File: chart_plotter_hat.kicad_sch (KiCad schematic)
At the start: 70 parts, among them J1 JST PH, J10 JST PH, J11 Qwiic, J2 JST PH, J3 40HAT, J4 JST PH, J5 JST PH, J6 JST PH, J7 JST PH, J8 Conn_02x03_Odd_Even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

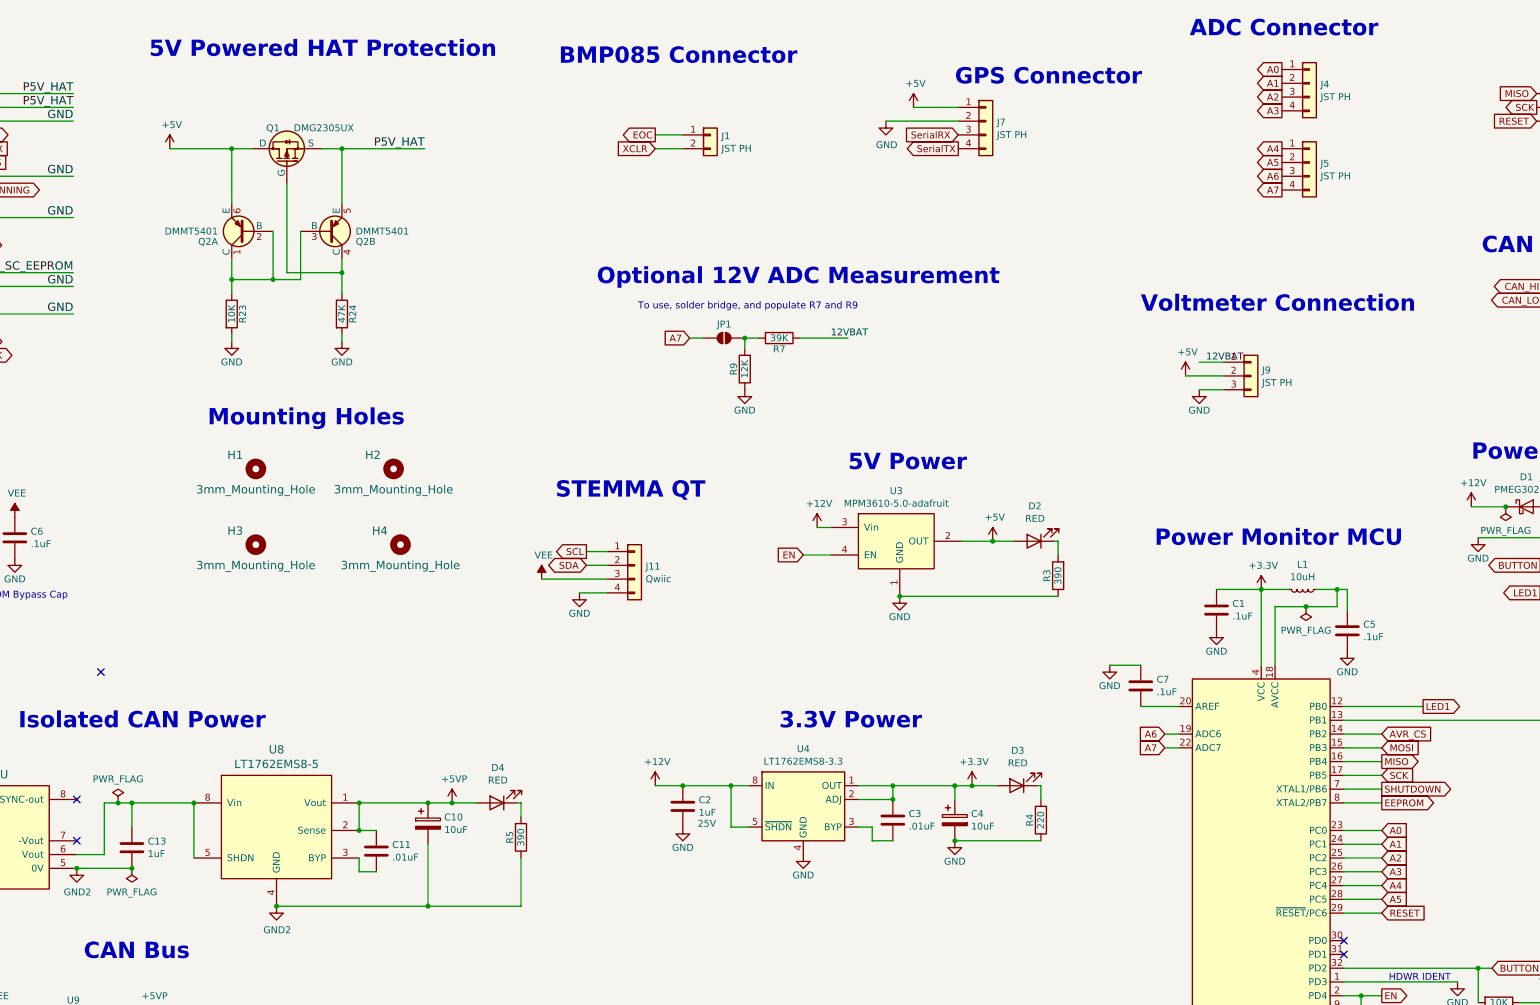
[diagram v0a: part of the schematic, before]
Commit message: Added solder jumpers for SCL/SDA
Removed BMP connector and associated routes
Can now connect QWIK connector to Pi or Atmega via jumpers
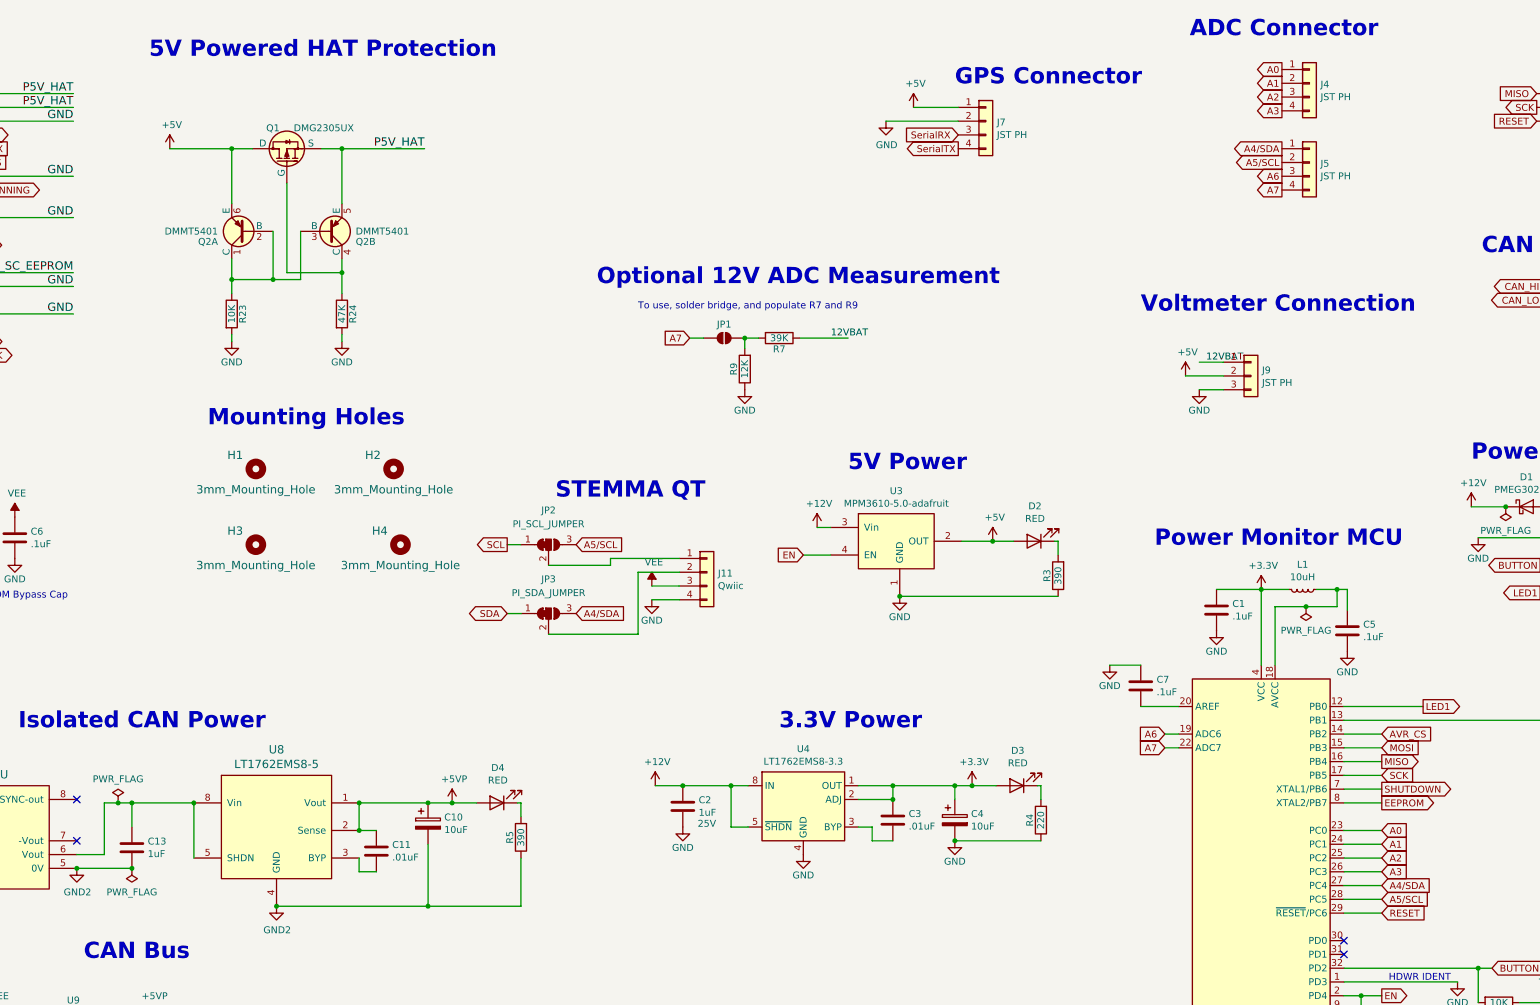
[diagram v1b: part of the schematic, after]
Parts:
- removed J1: JST PH, Connectors_JST:JST_PH_B2B-PH-K_02x2.00mm_Straight, symbol Connector_Generic:Conn_01x02
- added JP2: PI_SCL_JUMPER, Jumper:SolderJumper-3_P1.3mm_Bridged2Bar12_Pad1.0x1.5mm, symbol Jumper:SolderJumper_3_Bridged12
- added JP3: PI_SDA_JUMPER, Jumper:SolderJumper-3_P1.3mm_Bridged2Bar12_Pad1.0x1.5mm, symbol Jumper:SolderJumper_3_Bridged12
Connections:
- net SCL: now also JP2.1 (A); no longer J11.1 (Pin_1)
- net SDA: now also JP3.1 (A); no longer J11.2 (Pin_2)
- net A4 renamed A4/SDA
- net A4/SDA: now also JP3.3 (B)
- net A5 renamed A5/SCL
- net A5/SCL: now also JP2.3 (B)
- new net: J11.1 (Pin_1), JP2.2 (C)
- new net: J11.2 (Pin_2), JP3.2 (C)
- no-connect marks 28 -> 27
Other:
- note removed: "BMP085 Connector"
- moved on the sheet: J11

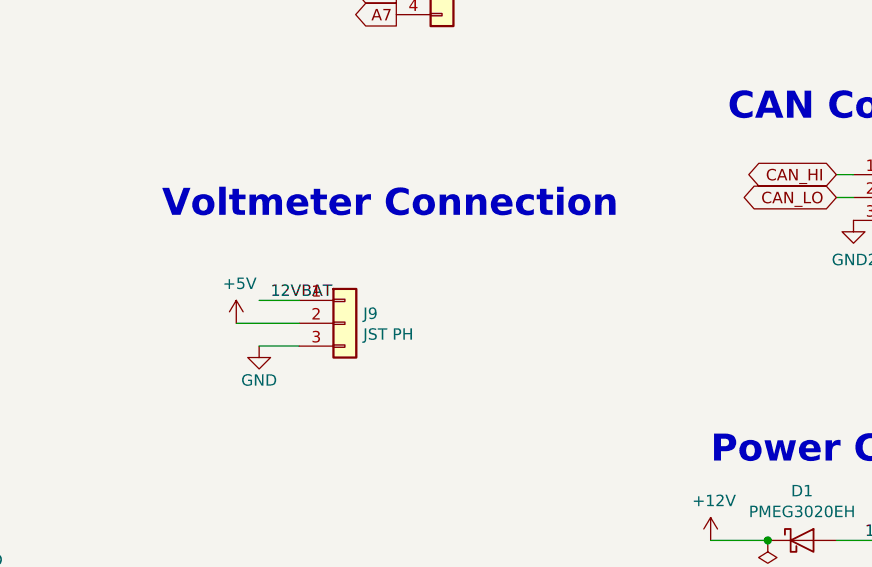
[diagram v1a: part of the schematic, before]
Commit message: Removed voltmeter connector and traces
Updated some trace routing
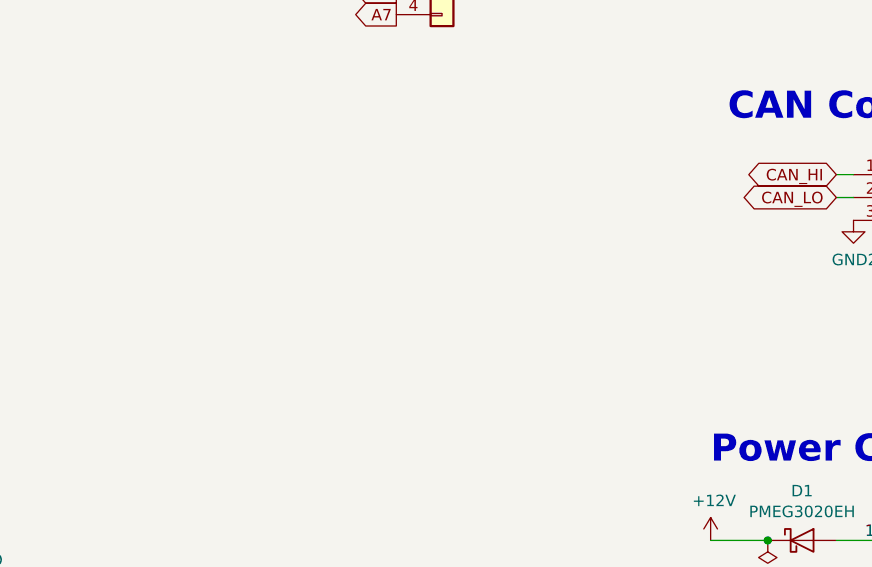
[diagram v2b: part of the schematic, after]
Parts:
- removed J9: JST PH, Connectors_JST:JST_PH_B3B-PH-K_03x2.00mm_Straight, symbol Connector_Generic:Conn_01x03
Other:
- note removed: "Voltmeter Connection"
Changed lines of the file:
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@@
 		)
 	)
-	(text "Voltmeter Connection"
-		(exclude_from_sim no)
-		(at 309.88 73.025 0)
-		(effects
-			(font
-				(size 2.9972 2.9972)
-				(thickness 0.5994)
-				(bold yes)
-			)
-			(justify left bottom)
-		)
-	)
 	(text "CAN Connector"
 		(exclude_from_sim no)
@@
 	(wire
 		(pts
-			(xy 325.12 86.995) (xy 320.675 86.995)
-		)
-		(stroke
-			(width 0)
-			(type default)
-		)
-	)
-	(wire
-		(pts
 			(xy 340.36 127) (xy 346.075 127)
 		)
@@
 	(wire
 		(pts
-			(xy 325.12 84.455) (xy 318.135 84.455)
-		)
-		(stroke
-			(width 0)
-			(type default)
-		)
-	)
-	(wire
-		(pts
 			(xy 82.55 40.005) (xy 91.44 40.005)
 		)
@@
 	(wire
 		(pts
-			(xy 325.12 81.915) (xy 320.675 81.915)
-		)
-		(stroke
-			(width 0)
-			(type default)
-		)
-	)
-	(wire
-		(pts
 			(xy 82.55 60.325) (xy 90.805 60.325)
 		)
@@
 		)
 	)
-	(label "12VBAT"
-		(at 321.945 81.915 0)
-		(effects
-			(font
-				(size 1.27 1.27)
-			)
-			(justify left bottom)
-		)
-	)
 	(label "GND"
 		(at 113.03 47.625 180)
@@
 	)
 	(symbol
-		(lib_id "Connector_Generic:Conn_01x03")
-		(at 330.2 84.455 0)
-		(unit 1)
-		(exclude_from_sim no)
-		(in_bom yes)
-		(on_board yes)
-		(dnp no)
-		(property "Reference" "J9"
-			(at 332.232 83.3882 0)
-			(effects
-				(font
-					(size 1.27 1.27)
-				)
-				(justify left)
-			)
-		)
-		(property "Value" "JST PH"
-			(at 332.232 85.6996 0)
-			(effects
-				(font
-					(size 1.27 1.27)
-				)
-				(justify left)
-			)
-		)
-		(property "Footprint" "Connectors_JST:JST_PH_B3B-PH-K_03x2.00mm_Straight"
-			(at 330.2 84.455 0)
-			(effects
-				(font
-					(size 1.27 1.27)
-				)
-				(hide yes)
-			)
-		)
-		(property "Datasheet" "~"
-			(at 330.2 84.455 0)
-			(effects
-				(font
-					(size 1.27 1.27)
-				)
-				(hide yes)
-			)
-		)
-		(property "Description" ""
-			(at 330.2 84.455 0)
-			(effects
-				(font
-					(size 1.27 1.27)
-				)
-			)
-		)
-		(pin "1"
-		)
-		(pin "2"
-		)
-		(pin "3"
-		)
-		(instances
-			(project ""
-				(path "/539f7589-5491-4018-9113-34d36da6b689"
-					(reference "J9")
-					(unit 1)
-				)
-			)
-		)
-	)
-	(symbol
 		(lib_id "Device:R")
 		(at 394.335 162.56 180)
@@
 	)
 	(symbol
-		(lib_id "power:GND")
-		(at 320.675 86.995 0)
-		(unit 1)
-		(exclude_from_sim no)
-		(in_bom yes)
-		(on_board yes)
-		(dnp no)
-		(property "Reference" "#PWR0119"
-			(at 320.675 93.345 0)
-			(effects
-				(font
-					(size 1.27 1.27)
-				)
-				(hide yes)
-			)
-		)
-		(property "Value" "GND"
-			(at 320.675 90.805 0)
-			(effects
-				(font
-					(size 1.27 1.27)
-				)
-			)
-		)
-		(property "Footprint" ""
-			(at 320.675 86.995 0)
-			(effects
-				(font
-					(size 1.27 1.27)
-				)
-			)
-		)
-		(property "Datasheet" ""
-			(at 320.675 86.995 0)
-			(effects
-				(font
-					(size 1.27 1.27)
-				)
-			)
-		)
-		(property "Description" ""
-			(at 320.675 86.995 0)
-			(effects
-				(font
-					(size 1.27 1.27)
-				)
-			)
-		)
-		(pin "1"
-		)
-		(instances
-			(project ""
-				(path "/539f7589-5491-4018-9113-34d36da6b689"
-					(reference "#PWR0119")
-					(unit 1)
-				)
-			)
-		)
-	)
-	(symbol
 		(lib_id "power:+5V")
 		(at 130.81 42.545 0)
@@
 					(unit 1)
 				)
-			)
-		)
-	)
-	(symbol
-		(lib_id "power:+5V")
-		(at 318.135 84.455 0)
-		(unit 1)
-		(exclude_from_sim no)
-		(in_bom yes)
-		(on_board yes)
-		(dnp no)
-		(property "Reference" "#PWR0124"
-			(at 318.135 88.265 0)
-			(effects
-				(font
-					(size 1.27 1.27)
-				)
-				(hide yes)
-			)
-		)
-		(property "Value" "+5V"
-			(at 318.516 80.0608 0)
-			(effects
-				(font
-					(size 1.27 1.27)
-				)
-			)
-		)
-		(property "Footprint" ""
-			(at 318.135 84.455 0)
-			(effects
-				(font
-					(size 1.27 1.27)
-				)
-				(hide yes)
-			)
-		)
-		(property "Datasheet" ""
-			(at 318.135 84.455 0)
-			(effects
-				(font
-					(size 1.27 1.27)
-				)
-				(hide yes)
-			)
-		)
-		(property "Description" ""
-			(at 318.135 84.455 0)
-			(effects
-				(font
-					(size 1.27 1.27)
-				)
-			)
-		)
-		(pin "1"
-		)
-		(instances
-			(project ""
-				(path "/539f7589-5491-4018-9113-34d36da6b689"
-					(reference "#PWR0124")
-					(unit 1)
-				)
